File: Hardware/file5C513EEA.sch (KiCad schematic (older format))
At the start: 80 parts, among them J10 IN_2, J11 IN_3, J12 PWM_CV, J13 EXT_CON, J4 OUT2_CON, J5 CUTOFF_CV, J6 SHAPE_CV, J7 SET_CV, J8 OUT1_CON, J9 IN_1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

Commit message: Generated STM32CubeMX code as a platformio project
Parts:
- RV5, RV6, RV7, RV8: symbol SID_Parts:BOURNS_PTL -> EuroSID-rescue:BOURNS_PTL-SID_Parts
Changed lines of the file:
@@
 -10V_REF_IO
 $Comp
-L SID_Parts:BOURNS_PTL RV5
+L EuroSID-rescue:BOURNS_PTL-SID_Parts RV5
 U 1 1 5BEA495C
 P 2200 700
+AR Path="/5BEA495C" Ref="RV5"  Part="1"
+AR Path="/5BFD63E3/5C513EEB/5BEA495C" Ref="RV5"  Part="1"
 F 0 "RV5" H 2112 496 50  0000 R CNN
 F 1 "ATTACK" H 2112 405 50  0000 R CNN
@@
 $EndComp
 $Comp
-L SID_Parts:BOURNS_PTL RV8
+L EuroSID-rescue:BOURNS_PTL-SID_Parts RV8
 U 1 1 5C03E468
 P 3350 700
+AR Path="/5C03E468" Ref="RV8"  Part="1"
+AR Path="/5BFD63E3/5C513EEB/5C03E468" Ref="RV8"  Part="1"
 F 0 "RV8" H 3262 496 50  0000 R CNN
 F 1 "RELEASE" H 3262 405 50  0000 R CNN
@@
 $EndComp
 $Comp
-L SID_Parts:BOURNS_PTL RV6
+L EuroSID-rescue:BOURNS_PTL-SID_Parts RV6
 U 1 1 5C057FF7
 P 2300 1800
+AR Path="/5C057FF7" Ref="RV6"  Part="1"
+AR Path="/5BFD63E3/5C513EEB/5C057FF7" Ref="RV6"  Part="1"
 F 0 "RV6" H 2212 1596 50  0000 R CNN
 F 1 "DECAY" H 2212 1505 50  0000 R CNN
@@
 $EndComp
 $Comp
-L SID_Parts:BOURNS_PTL RV7
+L EuroSID-rescue:BOURNS_PTL-SID_Parts RV7
 U 1 1 5C071B88
 P 2200 2900
+AR Path="/5C071B88" Ref="RV7"  Part="1"
+AR Path="/5BFD63E3/5C513EEB/5C071B88" Ref="RV7"  Part="1"
 F 0 "RV7" H 2112 2696 50  0000 R CNN
 F 1 "SUSTAIN" H 2112 2605 50  0000 R CNN

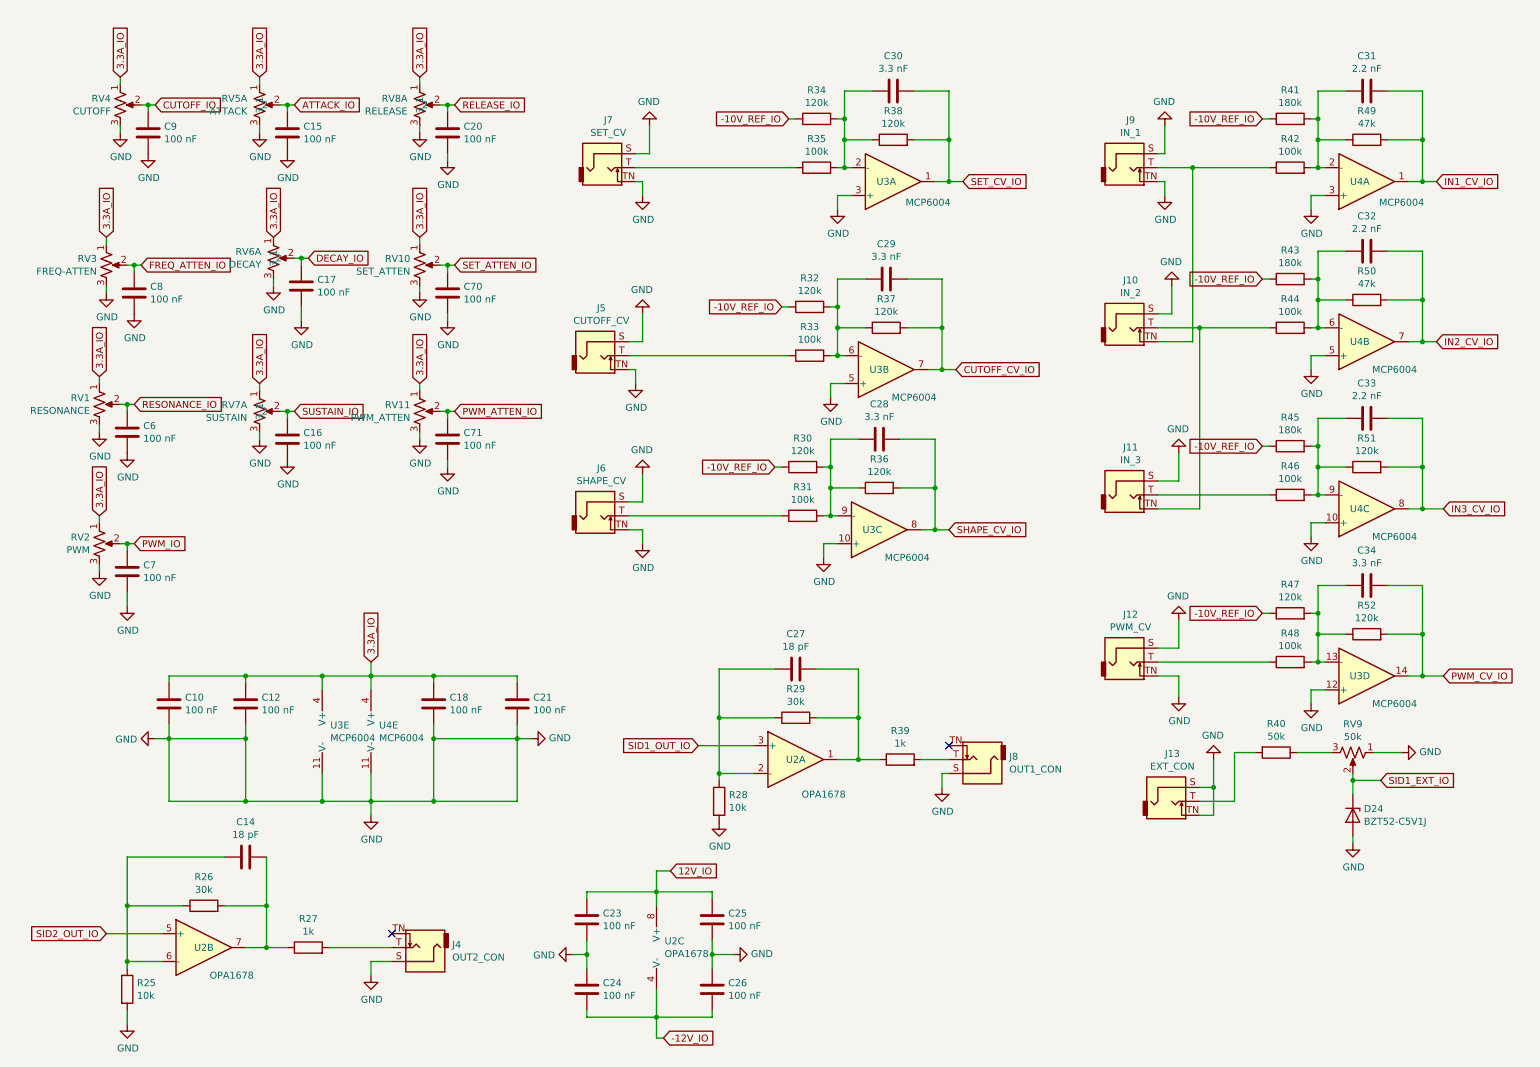
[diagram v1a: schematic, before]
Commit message: Cleaned up some traces, fixes #5
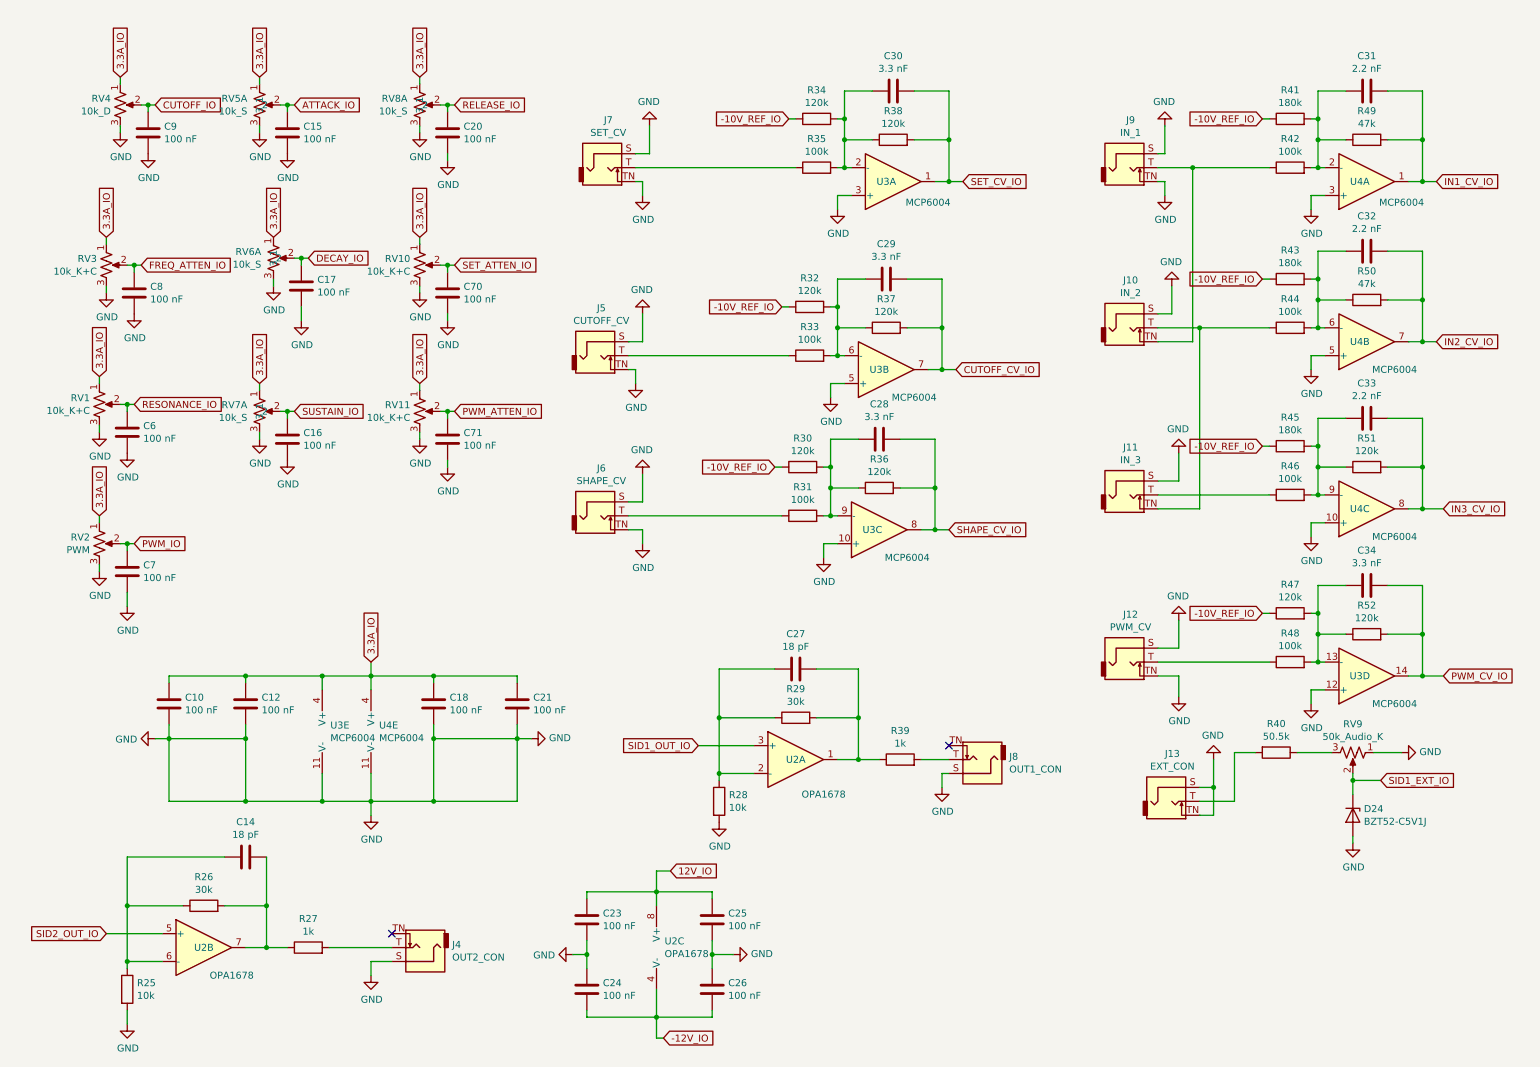
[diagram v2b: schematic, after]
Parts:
- R40: value 50k -> 50.5k
- RV1: value RESONANCE -> 10k_K+C
- RV10: value SET_ATTEN -> 10k_K+C
- RV11: value PWM_ATTEN -> 10k_K+C
- RV3: value FREQ-ATTEN -> 10k_K+C
- RV4: value CUTOFF -> 10k_D
- RV5: value ATTACK -> 10k_S
- RV6: value DECAY -> 10k_S
- RV7: value SUSTAIN -> 10k_S
- RV8: value RELEASE -> 10k_S
- RV9: value 50k -> 50k_Audio_K
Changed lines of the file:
@@
 AR Path="/5BFD63E3/5C513EEB/5C572178" Ref="RV4"  Part="1"
 F 0 "RV4" H 1132 996 50  0000 R CNN
-F 1 "CUTOFF" H 1132 905 50  0000 R CNN
+F 1 "10k_D" H 1132 905 50  0000 R CNN
 F 2 "Potentiometer_THT:Potentiometer_Bourns_PTV09A-1_Single_Vertical" H 1200 950 50  0001 C CNN
 F 3 "~" H 1200 950 50  0001 C CNN
@@
 AR Path="/5BFD63E3/5C513EEB/5C57218F" Ref="RV1"  Part="1"
 F 0 "RV1" H 982 3146 50  0000 R CNN
-F 1 "RESONANCE" H 982 3055 50  0000 R CNN
+F 1 "10k_K+C" H 982 3055 50  0000 R CNN
 F 2 "Potentiometer_THT:Potentiometer_Bourns_PTV09A-1_Single_Vertical" H 1050 3100 50  0001 C CNN
 F 3 "~" H 1050 3100 50  0001 C CNN
@@
 AR Path="/5BFD63E3/5C513EEB/5C572289" Ref="RV3"  Part="1"
 F 0 "RV3" H 1032 2146 50  0000 R CNN
-F 1 "FREQ-ATTEN" H 1032 2055 50  0000 R CNN
+F 1 "10k_K+C" H 1032 2055 50  0000 R CNN
 F 2 "Potentiometer_THT:Potentiometer_Bourns_PTV09A-1_Single_Vertical" H 1100 2100 50  0001 C CNN
 F 3 "~" H 1100 2100 50  0001 C CNN
@@
 AR Path="/5BFD63E3/5C513EEB/5C5D988B" Ref="RV9"  Part="1"
 F 0 "RV9" V 9845 5600 50  0000 C CNN
-F 1 "50k" V 9936 5600 50  0000 C CNN
+F 1 "50k_Audio_K" V 9936 5600 50  0000 C CNN
 F 2 "Potentiometer_THT:Potentiometer_Bourns_PTV09A-1_Single_Vertical" H 10050 5600 50  0001 C CNN
 F 3 "~" H 10050 5600 50  0001 C CNN
@@
 AR Path="/5BFD63E3/5C513EEB/5C5D98B2" Ref="R40"  Part="1"
 F 0 "R40" V 9293 5600 50  0000 C CNN
-F 1 "50k" V 9384 5600 50  0000 C CNN
+F 1 "50.5k" V 9384 5600 50  0000 C CNN
 F 2 "Resistor_SMD:R_0603_1608Metric" V 9430 5600 50  0001 C CNN
 F 3 "~" H 9500 5600 50  0001 C CNN
@@
 AR Path="/5BFD63E3/5C513EEB/5BF40470" Ref="RV11"  Part="1"
 F 0 "RV11" H 3282 3196 50  0000 R CNN
-F 1 "PWM_ATTEN" H 3282 3105 50  0000 R CNN
+F 1 "10k_K+C" H 3282 3105 50  0000 R CNN
 F 2 "Potentiometer_THT:Potentiometer_Bourns_PTV09A-1_Single_Vertical" H 3350 3150 50  0001 C CNN
 F 3 "~" H 3350 3150 50  0001 C CNN
@@
 AR Path="/5BFD63E3/5C513EEB/5BEA495C" Ref="RV5"  Part="1"
 F 0 "RV5" H 2112 496 50  0000 R CNN
-F 1 "ATTACK" H 2112 405 50  0000 R CNN
+F 1 "10k_S" H 2112 405 50  0000 R CNN
 F 2 "Potentiometer_THT:Potentiometer_Bourns_PTL20_Single_Slide" H 2200 700 50  0001 C CNN
 F 3 "" H 2200 700 50  0001 C CNN
@@
 AR Path="/5BFD63E3/5C513EEB/5BF0EB16" Ref="RV10"  Part="1"
 F 0 "RV10" H 3282 2146 50  0000 R CNN
-F 1 "SET_ATTEN" H 3282 2055 50  0000 R CNN
+F 1 "10k_K+C" H 3282 2055 50  0000 R CNN
 F 2 "Potentiometer_THT:Potentiometer_Bourns_PTV09A-1_Single_Vertical" H 3350 2100 50  0001 C CNN
 F 3 "~" H 3350 2100 50  0001 C CNN
@@
 AR Path="/5BFD63E3/5C513EEB/5C03E468" Ref="RV8"  Part="1"
 F 0 "RV8" H 3262 496 50  0000 R CNN
-F 1 "RELEASE" H 3262 405 50  0000 R CNN
+F 1 "10k_S" H 3262 405 50  0000 R CNN
 F 2 "Potentiometer_THT:Potentiometer_Bourns_PTL20_Single_Slide" H 3350 700 50  0001 C CNN
 F 3 "" H 3350 700 50  0001 C CNN
@@
 AR Path="/5BFD63E3/5C513EEB/5C057FF7" Ref="RV6"  Part="1"
 F 0 "RV6" H 2212 1596 50  0000 R CNN
-F 1 "DECAY" H 2212 1505 50  0000 R CNN
+F 1 "10k_S" H 2212 1505 50  0000 R CNN
 F 2 "Potentiometer_THT:Potentiometer_Bourns_PTL20_Single_Slide" H 2300 1800 50  0001 C CNN
 F 3 "" H 2300 1800 50  0001 C CNN
@@
 AR Path="/5BFD63E3/5C513EEB/5C071B88" Ref="RV7"  Part="1"
 F 0 "RV7" H 2112 2696 50  0000 R CNN
-F 1 "SUSTAIN" H 2112 2605 50  0000 R CNN
+F 1 "10k_S" H 2112 2605 50  0000 R CNN
 F 2 "Potentiometer_THT:Potentiometer_Bourns_PTL20_Single_Slide" H 2200 2900 50  0001 C CNN
 F 3 "" H 2200 2900 50  0001 C CNN
